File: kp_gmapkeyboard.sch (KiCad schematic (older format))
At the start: 20 parts, among them SW0 Encoder, SW1 Encoder, SW2 Encoder, SW3 Encoder, SW4 Encoder, U0 Teensy3.6, U1 MCP23017_SP

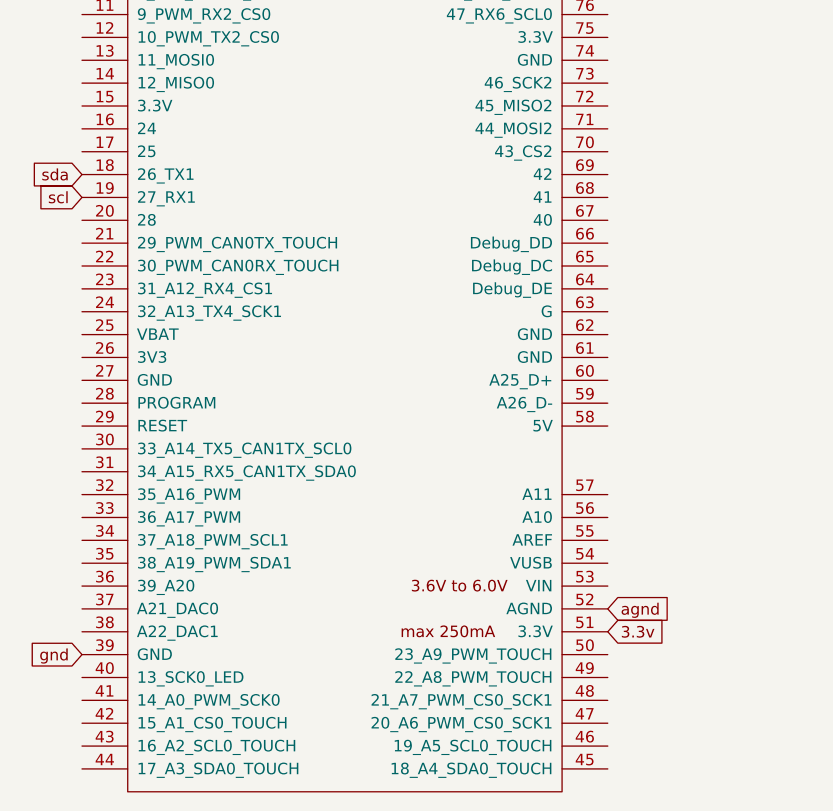
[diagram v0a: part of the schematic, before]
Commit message: fix sda/scl pins + update teensy3.6 symbol
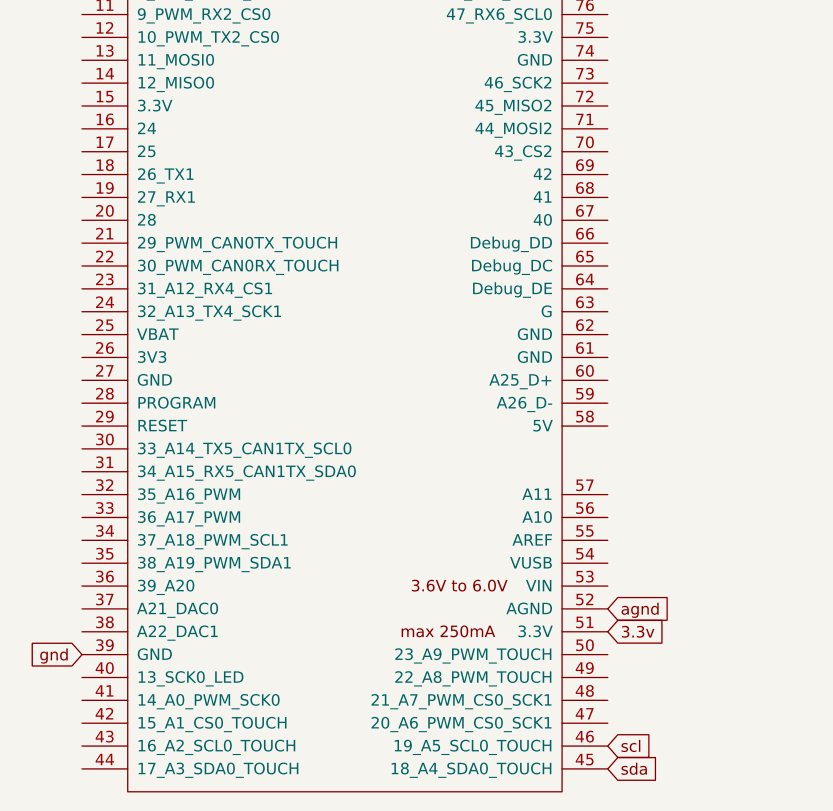
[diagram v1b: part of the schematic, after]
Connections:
- net scl: now also U0.46 (19_A5_SCL0_TOUCH); no longer U0.19 (27_RX1)
- net sda: now also U0.45 (18_A4_SDA0_TOUCH); no longer U0.18 (26_TX1)
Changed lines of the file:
@@
 Text GLabel 5700 1150 0    50   Input ~ 0
 scl
-Text GLabel 1150 2650 0    50   Input ~ 0
+Text GLabel 3450 5250 2    50   Input ~ 0
 sda
-Text GLabel 1150 2750 0    50   Input ~ 0
+Text GLabel 3450 5150 2    50   Input ~ 0
 scl
 Text GLabel 3450 4650 2    50   Input ~ 0

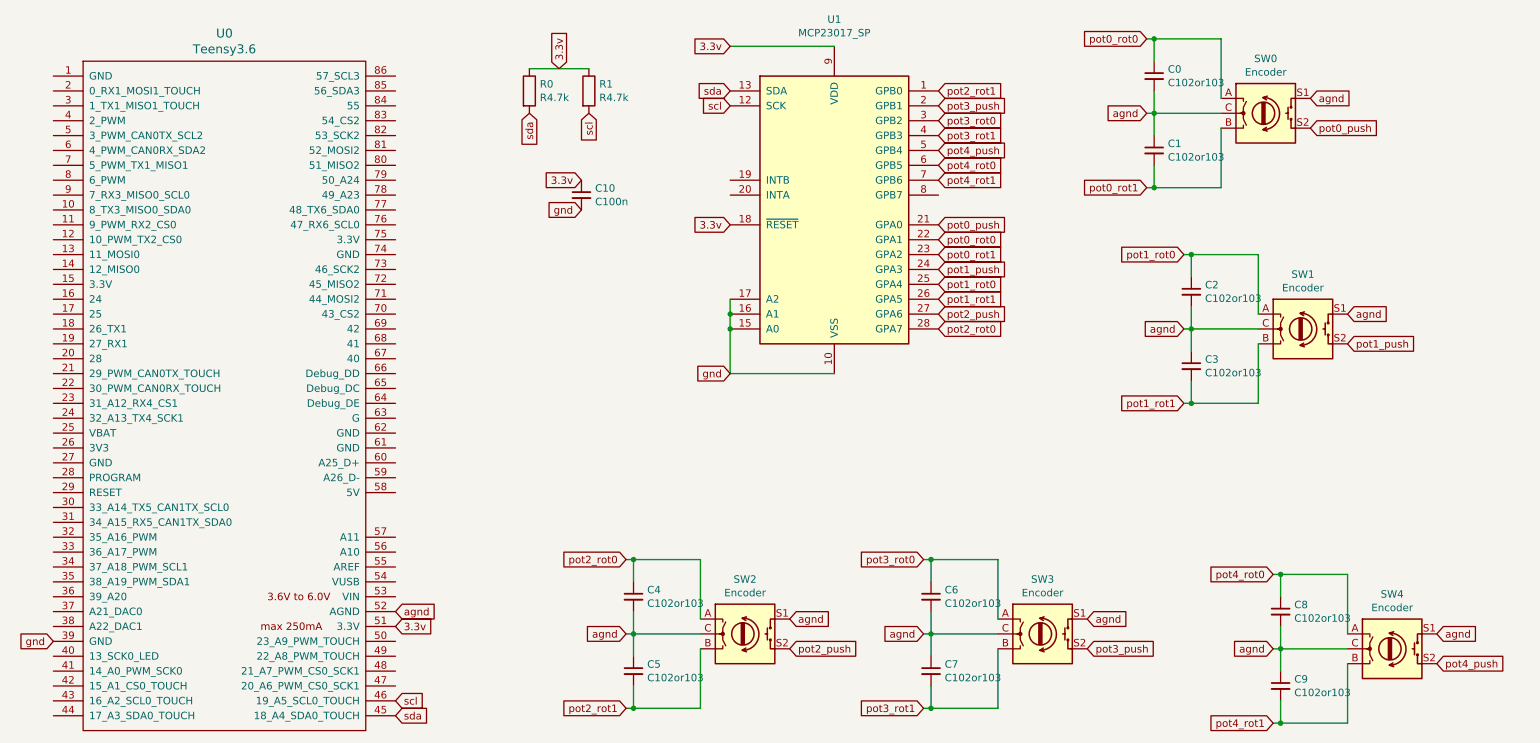
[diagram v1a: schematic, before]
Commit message: fix encoders pin order
when moving CW, the first pin "hit" by the turn is the lower pin number
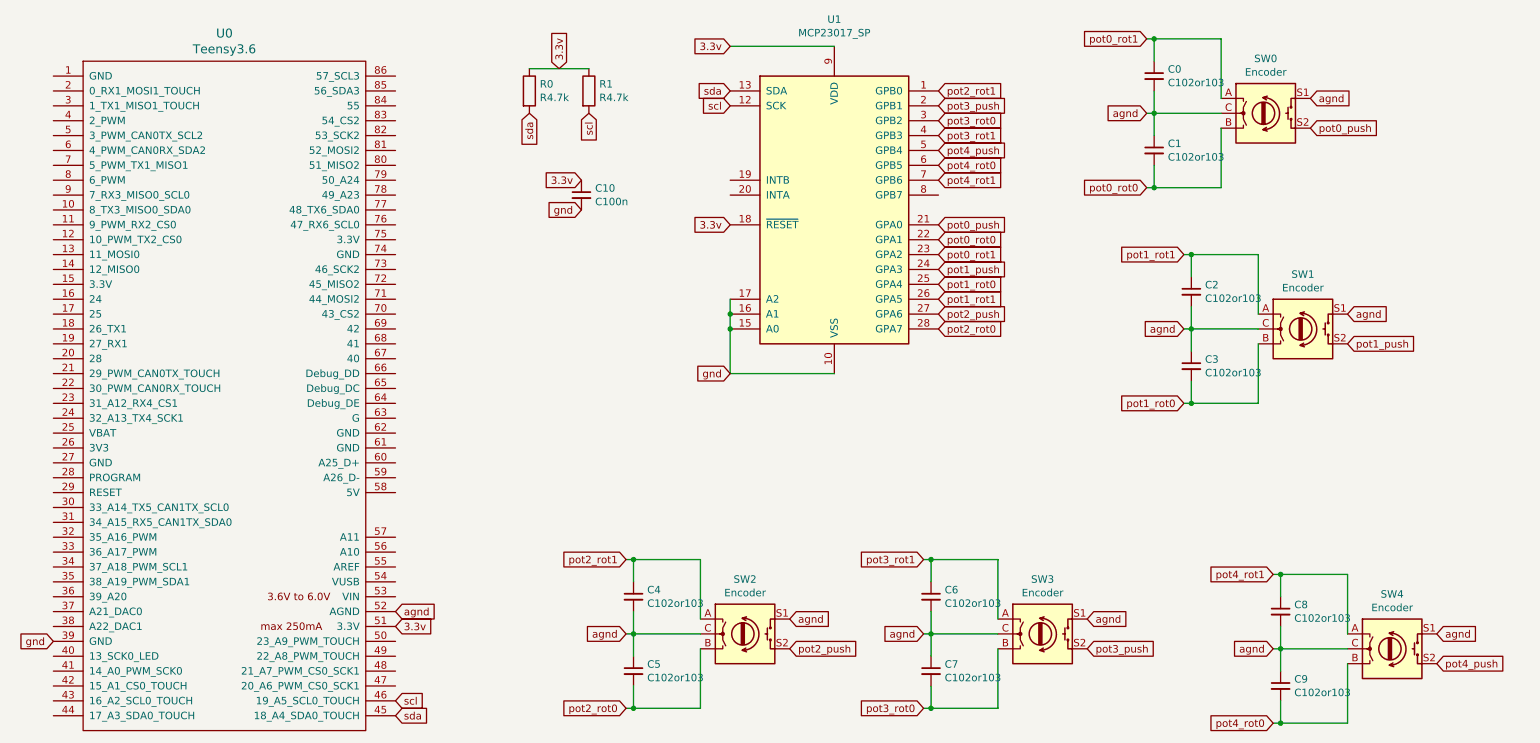
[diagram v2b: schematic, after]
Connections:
- net pot0_rot0: now also C1.2, SW0.B; no longer C0.1, SW0.A
- net pot0_rot1: now also C0.1, SW0.A; no longer C1.2, SW0.B
- net pot1_rot0: now also C3.2, SW1.B; no longer C2.1, SW1.A
- net pot1_rot1: now also C2.1, SW1.A; no longer C3.2, SW1.B
- net pot2_rot0: now also C5.2, SW2.B; no longer C4.1, SW2.A
- net pot2_rot1: now also C4.1, SW2.A; no longer C5.2, SW2.B
- net pot3_rot0: now also C7.2, SW3.B; no longer C6.1, SW3.A
- net pot3_rot1: now also C6.1, SW3.A; no longer C7.2, SW3.B
- net pot4_rot0: now also C9.2, SW4.B; no longer C8.1, SW4.A
- net pot4_rot1: now also C8.1, SW4.A; no longer C9.2, SW4.B
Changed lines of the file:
@@
 Text GLabel 8500 1200 0    50   Input ~ 0
 agnd
+Text GLabel 8500 1700 0    50   Input ~ 0
+pot0_rot0
 Text GLabel 8500 700  0    50   Input ~ 0
-pot0_rot0
-Text GLabel 8500 1700 0    50   Input ~ 0
 pot0_rot1
 Wire Wire Line
@@
 Text GLabel 8750 2650 0    50   Input ~ 0
 agnd
+Text GLabel 8750 3150 0    50   Input ~ 0
+pot1_rot0
 Text GLabel 8750 2150 0    50   Input ~ 0
-pot1_rot0
-Text GLabel 8750 3150 0    50   Input ~ 0
 pot1_rot1
 Wire Wire Line
@@
 Text GLabel 5000 4700 0    50   Input ~ 0
 agnd
+Text GLabel 5000 5200 0    50   Input ~ 0
+pot2_rot0
 Text GLabel 5000 4200 0    50   Input ~ 0
-pot2_rot0
-Text GLabel 5000 5200 0    50   Input ~ 0
 pot2_rot1
 Wire Wire Line
@@
 Text GLabel 7000 4700 0    50   Input ~ 0
 agnd
+Text GLabel 7000 5200 0    50   Input ~ 0
+pot3_rot0
 Text GLabel 7000 4200 0    50   Input ~ 0
-pot3_rot0
-Text GLabel 7000 5200 0    50   Input ~ 0
 pot3_rot1
 Wire Wire Line
@@
 Text GLabel 9350 4800 0    50   Input ~ 0
 agnd
+Text GLabel 9350 5300 0    50   Input ~ 0
+pot4_rot0
 Text GLabel 9350 4300 0    50   Input ~ 0
-pot4_rot0
-Text GLabel 9350 5300 0    50   Input ~ 0
 pot4_rot1
 Wire Wire Line

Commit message: disconnect push buttons, reorder connections to match real life
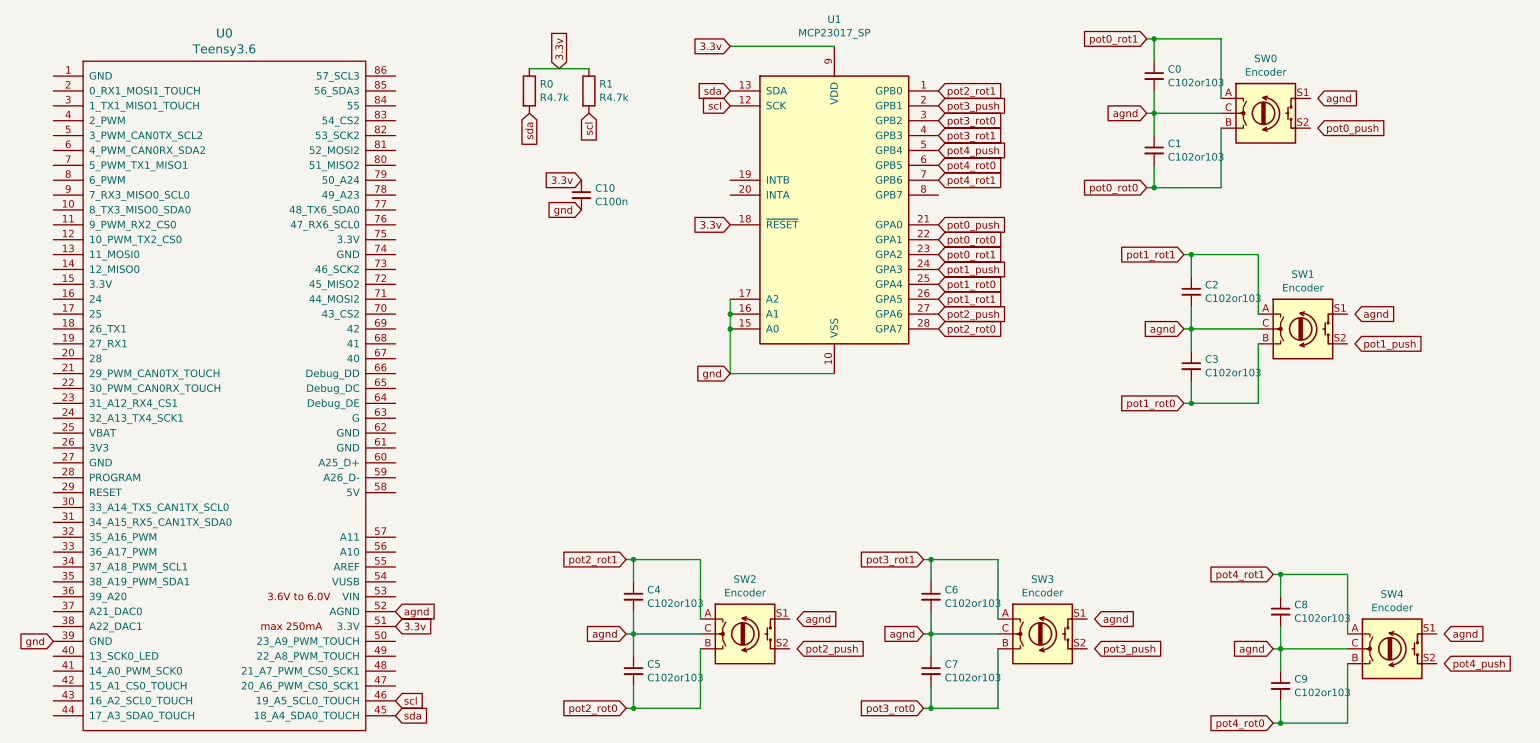
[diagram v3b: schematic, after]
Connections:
- net agnd: no longer SW0.S1, SW1.S1, SW2.S1, SW3.S1, SW4.S1
- net pot0_push: no longer SW0.S2
- net pot1_push: no longer SW1.S2
- net pot2_push: no longer SW2.S2
- net pot3_push: no longer SW3.S2
- net pot4_push: no longer SW4.S2
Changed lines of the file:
@@
 	1    0    0    -1
 $EndComp
-Text GLabel 9600 1100 2    50   Input ~ 0
-agnd
-Text GLabel 9600 1300 2    50   Input ~ 0
+Text GLabel 9650 1100 2    50   Input ~ 0
+agnd
+Text GLabel 9650 1300 2    50   Input ~ 0
 pot0_push
 Text GLabel 8500 1200 0    50   Input ~ 0
@@
 	1    0    0    -1
 $EndComp
-Text GLabel 9850 2550 2    50   Input ~ 0
-agnd
-Text GLabel 9850 2750 2    50   Input ~ 0
+Text GLabel 9900 2550 2    50   Input ~ 0
+agnd
+Text GLabel 9900 2750 2    50   Input ~ 0
 pot1_push
 Text GLabel 8750 2650 0    50   Input ~ 0
@@
 	1    0    0    -1
 $EndComp
-Text GLabel 6100 4600 2    50   Input ~ 0
-agnd
-Text GLabel 6100 4800 2    50   Input ~ 0
+Text GLabel 6150 4600 2    50   Input ~ 0
+agnd
+Text GLabel 6150 4800 2    50   Input ~ 0
 pot2_push
 Text GLabel 5000 4700 0    50   Input ~ 0
@@
 	1    0    0    -1
 $EndComp
-Text GLabel 8100 4600 2    50   Input ~ 0
-agnd
-Text GLabel 8100 4800 2    50   Input ~ 0
+Text GLabel 8150 4600 2    50   Input ~ 0
+agnd
+Text GLabel 8150 4800 2    50   Input ~ 0
 pot3_push
 Text GLabel 7000 4700 0    50   Input ~ 0
@@
 	1    0    0    -1
 $EndComp
-Text GLabel 10450 4700 2    50   Input ~ 0
-agnd
-Text GLabel 10450 4900 2    50   Input ~ 0
+Text GLabel 10500 4700 2    50   Input ~ 0
+agnd
+Text GLabel 10500 4900 2    50   Input ~ 0
 pot4_push
 Text GLabel 9350 4800 0    50   Input ~ 0
